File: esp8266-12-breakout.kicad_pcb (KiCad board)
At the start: 2 copper layers, 32.4 x 38.7 mm, 13 parts, among them P1 ftdi, P2 CONN_01X14, SW1 SW_PUSH, U1 AP1117D33

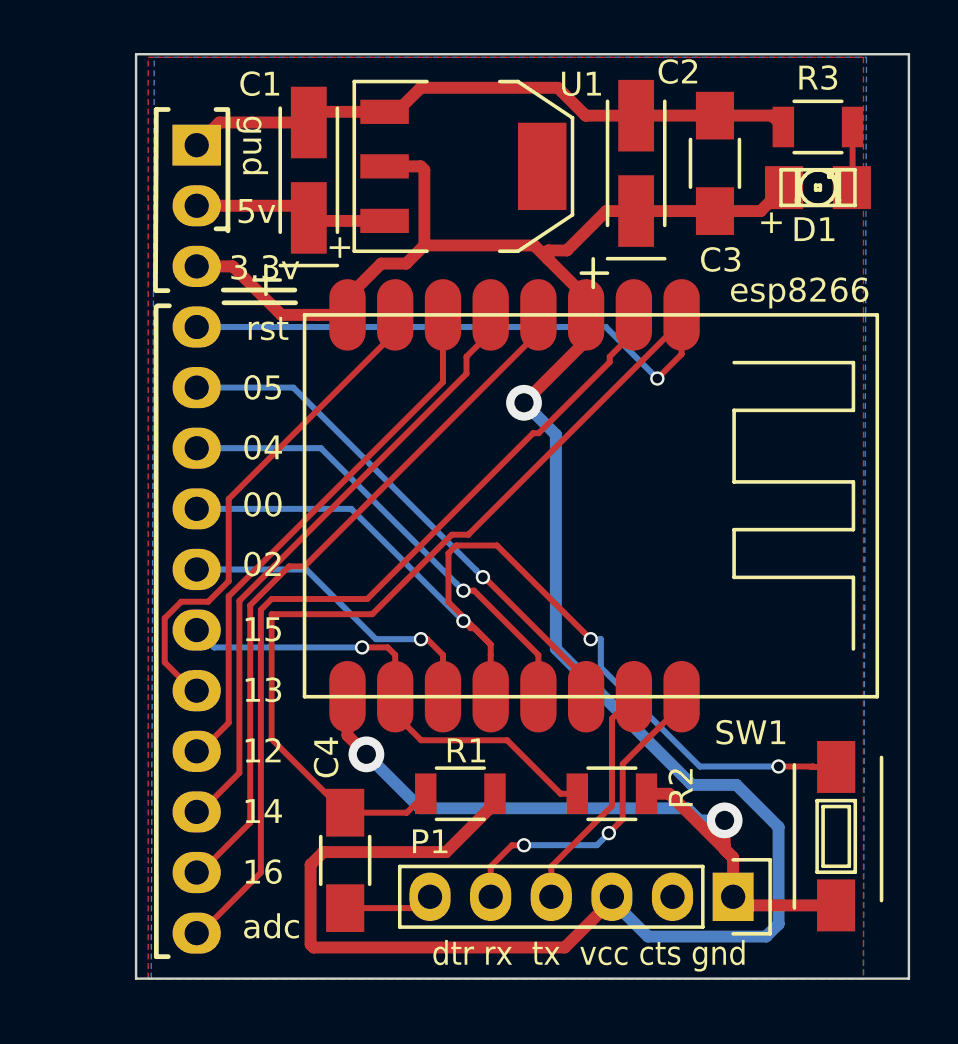
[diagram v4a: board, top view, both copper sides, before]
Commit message: v3 added pull up resistors for gpio0 & 2
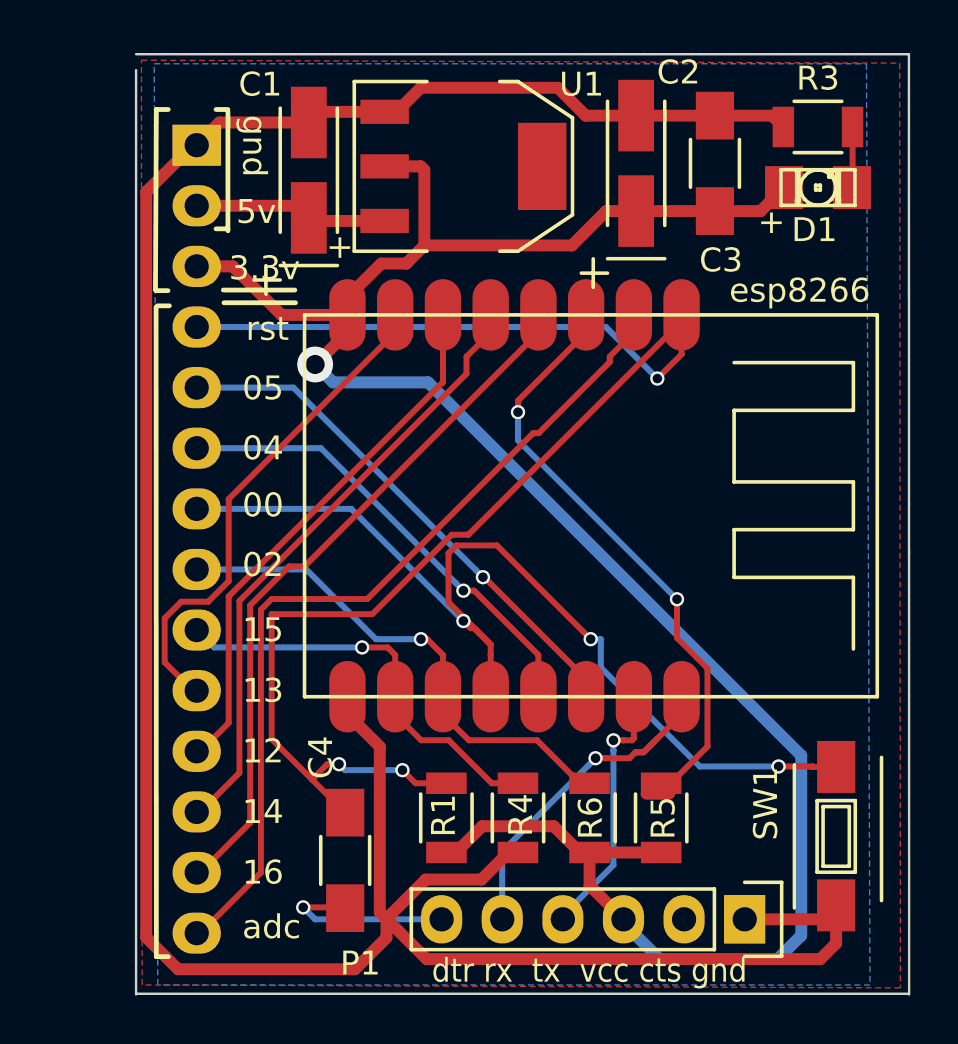
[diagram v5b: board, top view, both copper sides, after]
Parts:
- removed R2: 10k, Resistors_SMD:R_1206
- added R4: 10k, Resistors_SMD:R_1206, F.Cu at (128.9, 133.6)
- added R5: 10k, Resistors_SMD:R_1206, F.Cu at (131.9, 133.6)
- added R6: 10k, Resistors_SMD:R_1206, F.Cu at (125.9, 133.6)
- moved R1 1.17 mm to (122.9, 133.6), turned to 90 degrees
- moved P1 1.06 mm to (135.4, 137.8)
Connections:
- esp8266 pad 3: +3V3 -> /ch_pd
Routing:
- net GND: track 57.7 -> 114.5 mm, vias 2 -> 0
- net /ch_pd: track 0.00 -> 27.9 mm, vias 0 -> 2
- net +3V3: track 103.1 -> 92.4 mm
- net /gpio2: track 13.6 -> 21.6 mm
- net Net-(C4-Pad1): track 3.75 -> 7.78 mm, vias 0 -> 1
- net /gpio15: track 20.2 -> 17.6 mm
- net /reset: track 59.8 -> 62.4 mm, vias 1 -> 3
- net /rx: track 9.82 -> 11.0 mm, vias 0 -> 1
- net /tx: track 13.8 -> 14.9 mm, vias 2 -> 1
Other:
- board size 32.4 x 38.7 mm -> 32.4 x 39.4 mm
- board text added: "esp8266-12 v3 breakout board Matt Venn 2016"
- board text removed: "esp8266-12 v2 breakout board Matt Venn 2015"
